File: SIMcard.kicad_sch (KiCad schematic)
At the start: 9 parts, among them J8 1042240820

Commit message: Dual SIM version
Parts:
- renumbered R27 to R23, R28 to R24, R29 to R25
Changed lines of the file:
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@@
 		(in_pos_files yes)
 		(dnp no)
-		(property "Reference" "R27"
+		(property "Reference" "R23"
 			(at 134.112 71.12 90)
 			(show_name no)
@@
 			(project "GSMreceiver"
 				(path "/bbc92722-7b85-49e8-a662-589426df605a/0766f5ef-5d4e-4bb3-b73a-d8d6c795d8e3"
-					(reference "R30")
+					(reference "R26")
 					(unit 1)
 				)
 				(path "/bbc92722-7b85-49e8-a662-589426df605a/89f536d0-e840-48e9-a183-c973796594df"
-					(reference "R27")
+					(reference "R23")
 					(unit 1)
 				)
@@
 		(in_pos_files yes)
 		(dnp no)
-		(property "Reference" "R28"
+		(property "Reference" "R24"
 			(at 134.62 76.2 90)
 			(show_name no)
@@
 			(project "GSMreceiver"
 				(path "/bbc92722-7b85-49e8-a662-589426df605a/0766f5ef-5d4e-4bb3-b73a-d8d6c795d8e3"
-					(reference "R31")
+					(reference "R27")
 					(unit 1)
 				)
 				(path "/bbc92722-7b85-49e8-a662-589426df605a/89f536d0-e840-48e9-a183-c973796594df"
-					(reference "R28")
+					(reference "R24")
 					(unit 1)
 				)
@@
 		(in_pos_files yes)
 		(dnp no)
-		(property "Reference" "R29"
+		(property "Reference" "R25"
 			(at 134.62 81.28 90)
 			(show_name no)
@@
 			(project "GSMreceiver"
 				(path "/bbc92722-7b85-49e8-a662-589426df605a/0766f5ef-5d4e-4bb3-b73a-d8d6c795d8e3"
-					(reference "R32")
+					(reference "R28")
 					(unit 1)
 				)
 				(path "/bbc92722-7b85-49e8-a662-589426df605a/89f536d0-e840-48e9-a183-c973796594df"
-					(reference "R29")
-					(unit 1)
-				)
+					(reference "R25")
+					(unit 1)
+				)

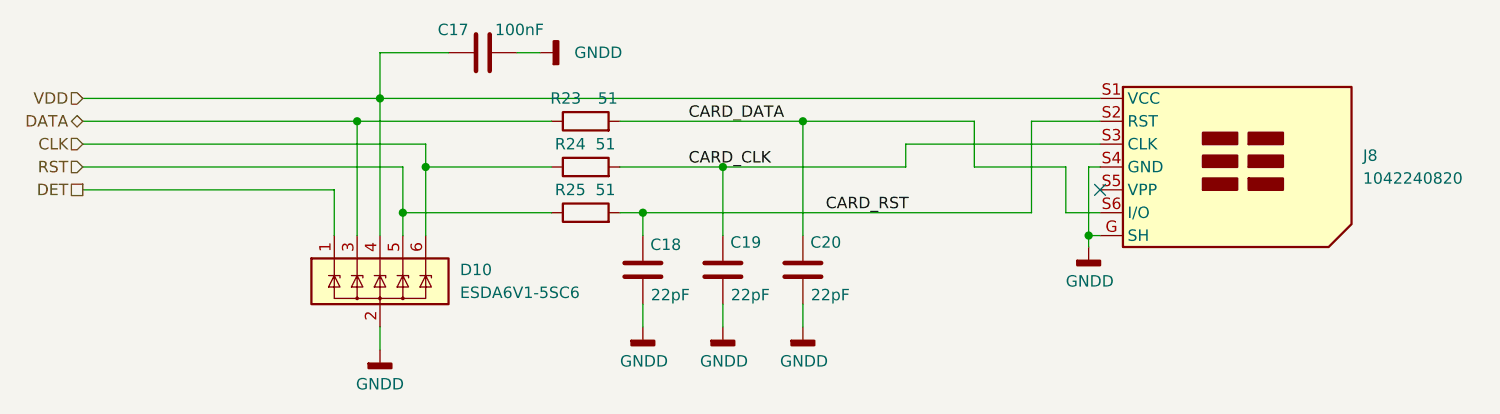
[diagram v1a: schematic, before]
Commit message: Replace SIM800C-DS with A7682E
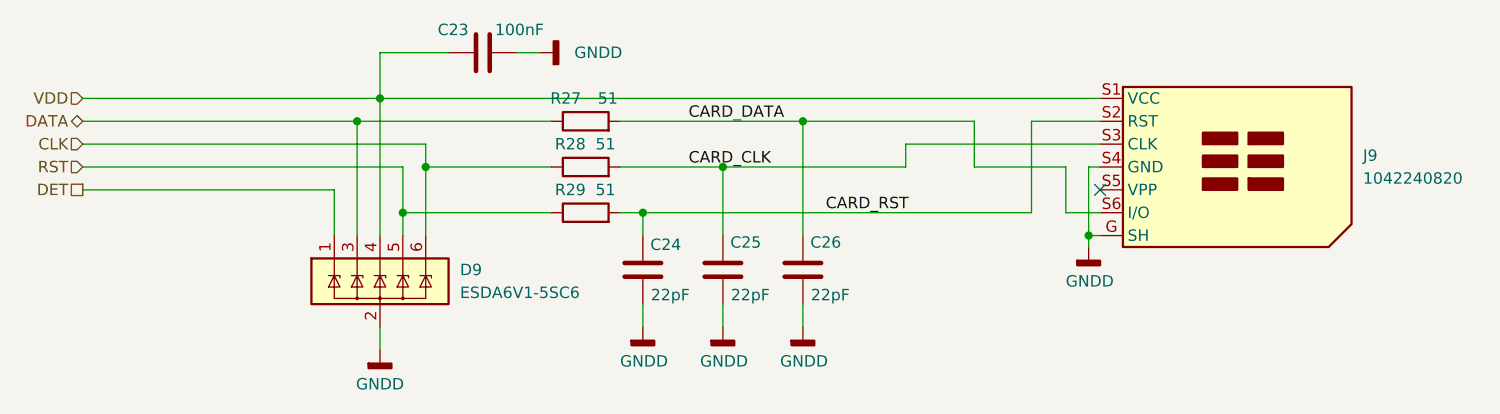
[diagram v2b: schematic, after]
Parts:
- renumbered C17 to C23, C18 to C24, C19 to C25, C20 to C26, D10 to D9, J8 to J9, R23 to R27, R24 to R28, R25 to R29
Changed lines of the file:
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@@
 		(in_pos_files yes)
 		(dnp no)
-		(property "Reference" "R23"
+		(property "Reference" "R27"
 			(at 134.112 71.12 90)
 			(show_name no)
@@
 			(project "GSMreceiver"
 				(path "/bbc92722-7b85-49e8-a662-589426df605a/0766f5ef-5d4e-4bb3-b73a-d8d6c795d8e3"
-					(reference "R26")
+					(reference "R30")
 					(unit 1)
 				)
 				(path "/bbc92722-7b85-49e8-a662-589426df605a/89f536d0-e840-48e9-a183-c973796594df"
-					(reference "R23")
+					(reference "R27")
 					(unit 1)
 				)
@@
 		(dnp no)
 		(fields_autoplaced yes)
-		(property "Reference" "#PWR038"
+		(property "Reference" "#PWR042"
 			(at 111.76 105.41 0)
 			(hide yes)
@@
 			(project "GSMreceiver"
 				(path "/bbc92722-7b85-49e8-a662-589426df605a/0766f5ef-5d4e-4bb3-b73a-d8d6c795d8e3"
-					(reference "#PWR044")
+					(reference "#PWR048")
 					(unit 1)
 				)
 				(path "/bbc92722-7b85-49e8-a662-589426df605a/89f536d0-e840-48e9-a183-c973796594df"
-					(reference "#PWR038")
+					(reference "#PWR042")
 					(unit 1)
 				)
@@
 		(in_pos_files yes)
 		(dnp no)
-		(property "Reference" "R24"
+		(property "Reference" "R28"
 			(at 134.62 76.2 90)
 			(show_name no)
@@
 			(project "GSMreceiver"
 				(path "/bbc92722-7b85-49e8-a662-589426df605a/0766f5ef-5d4e-4bb3-b73a-d8d6c795d8e3"
-					(reference "R27")
+					(reference "R31")
 					(unit 1)
 				)
 				(path "/bbc92722-7b85-49e8-a662-589426df605a/89f536d0-e840-48e9-a183-c973796594df"
-					(reference "R24")
+					(reference "R28")
 					(unit 1)
 				)
@@
 		(in_pos_files yes)
 		(dnp no)
-		(property "Reference" "#PWR043"
+		(property "Reference" "#PWR047"
 			(at 190.5 93.98 0)
 			(hide yes)
@@
 			(project "GSMreceiver"
 				(path "/bbc92722-7b85-49e8-a662-589426df605a/0766f5ef-5d4e-4bb3-b73a-d8d6c795d8e3"
-					(reference "#PWR049")
+					(reference "#PWR053")
 					(unit 1)
 				)
 				(path "/bbc92722-7b85-49e8-a662-589426df605a/89f536d0-e840-48e9-a183-c973796594df"
-					(reference "#PWR043")
+					(reference "#PWR047")
 					(unit 1)
 				)
@@
 		(dnp no)
 		(fields_autoplaced yes)
-		(property "Reference" "J8"
+		(property "Reference" "J9"
 			(at 220.98 77.4699 0)
 			(show_name no)
@@
 			(project "GSMreceiver"
 				(path "/bbc92722-7b85-49e8-a662-589426df605a/0766f5ef-5d4e-4bb3-b73a-d8d6c795d8e3"
+					(reference "J10")
+					(unit 1)
+				)
+				(path "/bbc92722-7b85-49e8-a662-589426df605a/89f536d0-e840-48e9-a183-c973796594df"
 					(reference "J9")
-					(unit 1)
-				)
-				(path "/bbc92722-7b85-49e8-a662-589426df605a/89f536d0-e840-48e9-a183-c973796594df"
-					(reference "J8")
 					(unit 1)
 				)
@@
 		(in_pos_files yes)
 		(dnp no)
-		(property "Reference" "#PWR042"
+		(property "Reference" "#PWR046"
 			(at 158.75 102.87 0)
 			(hide yes)
@@
 			(project "GSMreceiver"
 				(path "/bbc92722-7b85-49e8-a662-589426df605a/0766f5ef-5d4e-4bb3-b73a-d8d6c795d8e3"
-					(reference "#PWR048")
+					(reference "#PWR052")
 					(unit 1)
 				)
 				(path "/bbc92722-7b85-49e8-a662-589426df605a/89f536d0-e840-48e9-a183-c973796594df"
-					(reference "#PWR042")
+					(reference "#PWR046")
 					(unit 1)
 				)
@@
 		(in_pos_files yes)
 		(dnp no)
-		(property "Reference" "C19"
+		(property "Reference" "C25"
 			(at 152.4 87.122 0)
 			(show_name no)
@@
 			(project "GSMreceiver"
 				(path "/bbc92722-7b85-49e8-a662-589426df605a/0766f5ef-5d4e-4bb3-b73a-d8d6c795d8e3"
-					(reference "C23")
+					(reference "C29")
 					(unit 1)
 				)
 				(path "/bbc92722-7b85-49e8-a662-589426df605a/89f536d0-e840-48e9-a183-c973796594df"
-					(reference "C19")
+					(reference "C25")
 					(unit 1)
 				)
@@
 		(dnp no)
 		(fields_autoplaced yes)
-		(property "Reference" "#PWR039"
+		(property "Reference" "#PWR043"
 			(at 135.89 66.04 0)
 			(hide yes)
@@
 			(project "GSMreceiver"
 				(path "/bbc92722-7b85-49e8-a662-589426df605a/0766f5ef-5d4e-4bb3-b73a-d8d6c795d8e3"
-					(reference "#PWR045")
+					(reference "#PWR049")
 					(unit 1)
 				)
 				(path "/bbc92722-7b85-49e8-a662-589426df605a/89f536d0-e840-48e9-a183-c973796594df"
-					(reference "#PWR039")
+					(reference "#PWR043")
 					(unit 1)
 				)
@@
 		(in_pos_files yes)
 		(dnp no)
-		(property "Reference" "C17"
+		(property "Reference" "C23"
 			(at 119.888 63.5 90)
 			(show_name no)
@@
 			(project "GSMreceiver"
 				(path "/bbc92722-7b85-49e8-a662-589426df605a/0766f5ef-5d4e-4bb3-b73a-d8d6c795d8e3"
-					(reference "C21")
+					(reference "C27")
 					(unit 1)
 				)
 				(path "/bbc92722-7b85-49e8-a662-589426df605a/89f536d0-e840-48e9-a183-c973796594df"
-					(reference "C17")
+					(reference "C23")
 					(unit 1)
 				)
@@
 		(in_pos_files yes)
 		(dnp no)
-		(property "Reference" "C18"
+		(property "Reference" "C24"
 			(at 143.51 87.376 0)
 			(show_name no)
@@
 			(project "GSMreceiver"
 				(path "/bbc92722-7b85-49e8-a662-589426df605a/0766f5ef-5d4e-4bb3-b73a-d8d6c795d8e3"
-					(reference "C22")
+					(reference "C28")
 					(unit 1)
 				)
 				(path "/bbc92722-7b85-49e8-a662-589426df605a/89f536d0-e840-48e9-a183-c973796594df"
-					(reference "C18")
+					(reference "C24")
 					(unit 1)
 				)
@@
 		(dnp no)
 		(fields_autoplaced yes)
-		(property "Reference" "D10"
+		(property "Reference" "D9"
 			(at 120.65 90.1699 0)
 			(show_name no)
@@
 			(project "GSMreceiver"
 				(path "/bbc92722-7b85-49e8-a662-589426df605a/0766f5ef-5d4e-4bb3-b73a-d8d6c795d8e3"
-					(reference "D11")
+					(reference "D10")
 					(unit 1)
 				)
 				(path "/bbc92722-7b85-49e8-a662-589426df605a/89f536d0-e840-48e9-a183-c973796594df"
-					(reference "D10")
+					(reference "D9")
 					(unit 1)
 				)
@@
 		(in_pos_files yes)
 		(dnp no)
-		(property "Reference" "#PWR041"
+		(property "Reference" "#PWR045"
 			(at 149.86 102.87 0)
 			(hide yes)
@@
 			(project "GSMreceiver"
 				(path "/bbc92722-7b85-49e8-a662-589426df605a/0766f5ef-5d4e-4bb3-b73a-d8d6c795d8e3"
-					(reference "#PWR047")
+					(reference "#PWR051")
 					(unit 1)
 				)
 				(path "/bbc92722-7b85-49e8-a662-589426df605a/89f536d0-e840-48e9-a183-c973796594df"
-					(reference "#PWR041")
+					(reference "#PWR045")
 					(unit 1)
 				)
@@
 		(in_pos_files yes)
 		(dnp no)
-		(property "Reference" "C20"
+		(property "Reference" "C26"
 			(at 161.29 87.122 0)
 			(show_name no)
@@
 			(project "GSMreceiver"
 				(path "/bbc92722-7b85-49e8-a662-589426df605a/0766f5ef-5d4e-4bb3-b73a-d8d6c795d8e3"
-					(reference "C24")
+					(reference "C30")
 					(unit 1)
 				)
 				(path "/bbc92722-7b85-49e8-a662-589426df605a/89f536d0-e840-48e9-a183-c973796594df"
-					(reference "C20")
+					(reference "C26")
 					(unit 1)
 				)
@@
 		(in_pos_files yes)
 		(dnp no)
-		(property "Reference" "#PWR040"
+		(property "Reference" "#PWR044"
 			(at 140.97 102.87 0)
 			(hide yes)
@@
 			(project "GSMreceiver"
 				(path "/bbc92722-7b85-49e8-a662-589426df605a/0766f5ef-5d4e-4bb3-b73a-d8d6c795d8e3"
-					(reference "#PWR046")
+					(reference "#PWR050")
 					(unit 1)
 				)
 				(path "/bbc92722-7b85-49e8-a662-589426df605a/89f536d0-e840-48e9-a183-c973796594df"
-					(reference "#PWR040")
+					(reference "#PWR044")
 					(unit 1)
 				)
@@
 		(in_pos_files yes)
 		(dnp no)
-		(property "Reference" "R25"
+		(property "Reference" "R29"
 			(at 134.62 81.28 90)
 			(show_name no)
@@
 			(project "GSMreceiver"
 				(path "/bbc92722-7b85-49e8-a662-589426df605a/0766f5ef-5d4e-4bb3-b73a-d8d6c795d8e3"
-					(reference "R28")
+					(reference "R32")
 					(unit 1)
 				)
 				(path "/bbc92722-7b85-49e8-a662-589426df605a/89f536d0-e840-48e9-a183-c973796594df"
-					(reference "R25")
-					(unit 1)
-				)
+					(reference "R29")
+					(unit 1)
+				)

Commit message: USB connector inversion fix
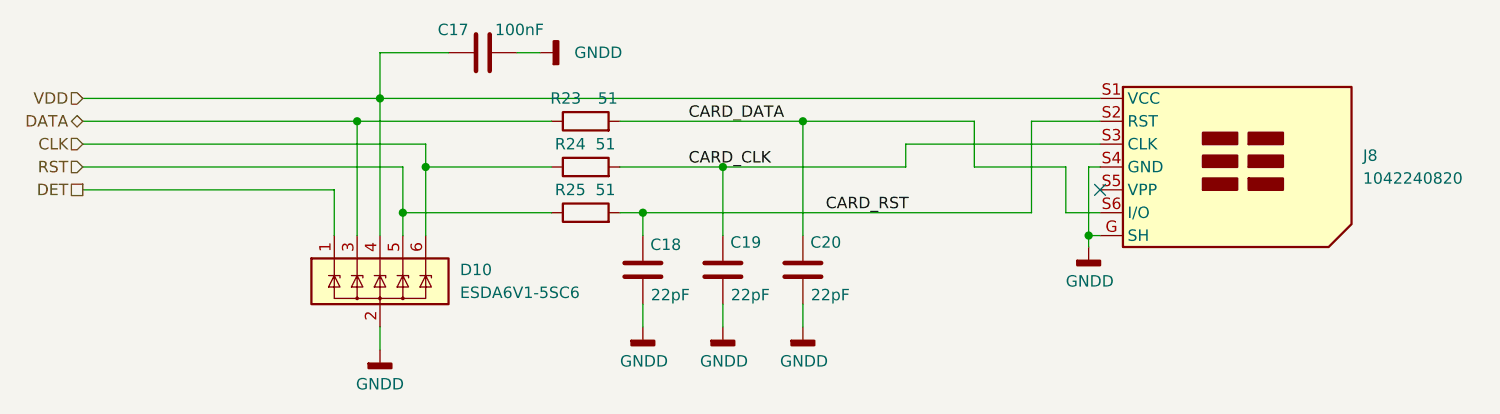
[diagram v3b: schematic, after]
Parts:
- renumbered C23 to C17, C24 to C18, C25 to C19, C26 to C20, D9 to D10, J9 to J8, R27 to R23, R28 to R24, R29 to R25
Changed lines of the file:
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@@
 		(in_pos_files yes)
 		(dnp no)
-		(property "Reference" "R27"
+		(property "Reference" "R23"
 			(at 134.112 71.12 90)
 			(show_name no)
@@
 			(project "GSMreceiver"
 				(path "/bbc92722-7b85-49e8-a662-589426df605a/0766f5ef-5d4e-4bb3-b73a-d8d6c795d8e3"
-					(reference "R30")
+					(reference "R26")
 					(unit 1)
 				)
 				(path "/bbc92722-7b85-49e8-a662-589426df605a/89f536d0-e840-48e9-a183-c973796594df"
-					(reference "R27")
+					(reference "R23")
 					(unit 1)
 				)
@@
 		(dnp no)
 		(fields_autoplaced yes)
-		(property "Reference" "#PWR042"
+		(property "Reference" "#PWR038"
 			(at 111.76 105.41 0)
 			(hide yes)
@@
 			(project "GSMreceiver"
 				(path "/bbc92722-7b85-49e8-a662-589426df605a/0766f5ef-5d4e-4bb3-b73a-d8d6c795d8e3"
-					(reference "#PWR048")
+					(reference "#PWR044")
 					(unit 1)
 				)
 				(path "/bbc92722-7b85-49e8-a662-589426df605a/89f536d0-e840-48e9-a183-c973796594df"
-					(reference "#PWR042")
+					(reference "#PWR038")
 					(unit 1)
 				)
@@
 		(in_pos_files yes)
 		(dnp no)
-		(property "Reference" "R28"
+		(property "Reference" "R24"
 			(at 134.62 76.2 90)
 			(show_name no)
@@
 			(project "GSMreceiver"
 				(path "/bbc92722-7b85-49e8-a662-589426df605a/0766f5ef-5d4e-4bb3-b73a-d8d6c795d8e3"
-					(reference "R31")
+					(reference "R27")
 					(unit 1)
 				)
 				(path "/bbc92722-7b85-49e8-a662-589426df605a/89f536d0-e840-48e9-a183-c973796594df"
-					(reference "R28")
+					(reference "R24")
 					(unit 1)
 				)
@@
 		(in_pos_files yes)
 		(dnp no)
-		(property "Reference" "#PWR047"
+		(property "Reference" "#PWR043"
 			(at 190.5 93.98 0)
 			(hide yes)
@@
 			(project "GSMreceiver"
 				(path "/bbc92722-7b85-49e8-a662-589426df605a/0766f5ef-5d4e-4bb3-b73a-d8d6c795d8e3"
-					(reference "#PWR053")
+					(reference "#PWR049")
 					(unit 1)
 				)
 				(path "/bbc92722-7b85-49e8-a662-589426df605a/89f536d0-e840-48e9-a183-c973796594df"
-					(reference "#PWR047")
+					(reference "#PWR043")
 					(unit 1)
 				)
@@
 		(dnp no)
 		(fields_autoplaced yes)
-		(property "Reference" "J9"
+		(property "Reference" "J8"
 			(at 220.98 77.4699 0)
 			(show_name no)
@@
 			(project "GSMreceiver"
 				(path "/bbc92722-7b85-49e8-a662-589426df605a/0766f5ef-5d4e-4bb3-b73a-d8d6c795d8e3"
-					(reference "J10")
+					(reference "J9")
 					(unit 1)
 				)
 				(path "/bbc92722-7b85-49e8-a662-589426df605a/89f536d0-e840-48e9-a183-c973796594df"
-					(reference "J9")
+					(reference "J8")
 					(unit 1)
 				)
@@
 		(in_pos_files yes)
 		(dnp no)
-		(property "Reference" "#PWR046"
+		(property "Reference" "#PWR042"
 			(at 158.75 102.87 0)
 			(hide yes)
@@
 			(project "GSMreceiver"
 				(path "/bbc92722-7b85-49e8-a662-589426df605a/0766f5ef-5d4e-4bb3-b73a-d8d6c795d8e3"
-					(reference "#PWR052")
+					(reference "#PWR048")
 					(unit 1)
 				)
 				(path "/bbc92722-7b85-49e8-a662-589426df605a/89f536d0-e840-48e9-a183-c973796594df"
-					(reference "#PWR046")
+					(reference "#PWR042")
 					(unit 1)
 				)
@@
 		(in_pos_files yes)
 		(dnp no)
-		(property "Reference" "C25"
+		(property "Reference" "C19"
 			(at 152.4 87.122 0)
 			(show_name no)
@@
 			(project "GSMreceiver"
 				(path "/bbc92722-7b85-49e8-a662-589426df605a/0766f5ef-5d4e-4bb3-b73a-d8d6c795d8e3"
-					(reference "C29")
+					(reference "C23")
 					(unit 1)
 				)
 				(path "/bbc92722-7b85-49e8-a662-589426df605a/89f536d0-e840-48e9-a183-c973796594df"
-					(reference "C25")
+					(reference "C19")
 					(unit 1)
 				)
@@
 		(dnp no)
 		(fields_autoplaced yes)
-		(property "Reference" "#PWR043"
+		(property "Reference" "#PWR039"
 			(at 135.89 66.04 0)
 			(hide yes)
@@
 			(project "GSMreceiver"
 				(path "/bbc92722-7b85-49e8-a662-589426df605a/0766f5ef-5d4e-4bb3-b73a-d8d6c795d8e3"
-					(reference "#PWR049")
+					(reference "#PWR045")
 					(unit 1)
 				)
 				(path "/bbc92722-7b85-49e8-a662-589426df605a/89f536d0-e840-48e9-a183-c973796594df"
-					(reference "#PWR043")
+					(reference "#PWR039")
 					(unit 1)
 				)
@@
 		(in_pos_files yes)
 		(dnp no)
-		(property "Reference" "C23"
+		(property "Reference" "C17"
 			(at 119.888 63.5 90)
 			(show_name no)
@@
 			(project "GSMreceiver"
 				(path "/bbc92722-7b85-49e8-a662-589426df605a/0766f5ef-5d4e-4bb3-b73a-d8d6c795d8e3"
-					(reference "C27")
+					(reference "C21")
 					(unit 1)
 				)
 				(path "/bbc92722-7b85-49e8-a662-589426df605a/89f536d0-e840-48e9-a183-c973796594df"
-					(reference "C23")
+					(reference "C17")
 					(unit 1)
 				)
@@
 		(in_pos_files yes)
 		(dnp no)
-		(property "Reference" "C24"
+		(property "Reference" "C18"
 			(at 143.51 87.376 0)
 			(show_name no)
@@
 			(project "GSMreceiver"
 				(path "/bbc92722-7b85-49e8-a662-589426df605a/0766f5ef-5d4e-4bb3-b73a-d8d6c795d8e3"
-					(reference "C28")
+					(reference "C22")
 					(unit 1)
 				)
 				(path "/bbc92722-7b85-49e8-a662-589426df605a/89f536d0-e840-48e9-a183-c973796594df"
-					(reference "C24")
+					(reference "C18")
 					(unit 1)
 				)
@@
 		(dnp no)
 		(fields_autoplaced yes)
-		(property "Reference" "D9"
+		(property "Reference" "D10"
 			(at 120.65 90.1699 0)
 			(show_name no)
@@
 			(project "GSMreceiver"
 				(path "/bbc92722-7b85-49e8-a662-589426df605a/0766f5ef-5d4e-4bb3-b73a-d8d6c795d8e3"
+					(reference "D11")
+					(unit 1)
+				)
+				(path "/bbc92722-7b85-49e8-a662-589426df605a/89f536d0-e840-48e9-a183-c973796594df"
 					(reference "D10")
-					(unit 1)
-				)
-				(path "/bbc92722-7b85-49e8-a662-589426df605a/89f536d0-e840-48e9-a183-c973796594df"
-					(reference "D9")
 					(unit 1)
 				)
@@
 		(in_pos_files yes)
 		(dnp no)
-		(property "Reference" "#PWR045"
+		(property "Reference" "#PWR041"
 			(at 149.86 102.87 0)
 			(hide yes)
@@
 			(project "GSMreceiver"
 				(path "/bbc92722-7b85-49e8-a662-589426df605a/0766f5ef-5d4e-4bb3-b73a-d8d6c795d8e3"
-					(reference "#PWR051")
+					(reference "#PWR047")
 					(unit 1)
 				)
 				(path "/bbc92722-7b85-49e8-a662-589426df605a/89f536d0-e840-48e9-a183-c973796594df"
-					(reference "#PWR045")
+					(reference "#PWR041")
 					(unit 1)
 				)
@@
 		(in_pos_files yes)
 		(dnp no)
-		(property "Reference" "C26"
+		(property "Reference" "C20"
 			(at 161.29 87.122 0)
 			(show_name no)
@@
 			(project "GSMreceiver"
 				(path "/bbc92722-7b85-49e8-a662-589426df605a/0766f5ef-5d4e-4bb3-b73a-d8d6c795d8e3"
-					(reference "C30")
+					(reference "C24")
 					(unit 1)
 				)
 				(path "/bbc92722-7b85-49e8-a662-589426df605a/89f536d0-e840-48e9-a183-c973796594df"
-					(reference "C26")
+					(reference "C20")
 					(unit 1)
 				)
@@
 		(in_pos_files yes)
 		(dnp no)
-		(property "Reference" "#PWR044"
+		(property "Reference" "#PWR040"
 			(at 140.97 102.87 0)
 			(hide yes)
@@
 			(project "GSMreceiver"
 				(path "/bbc92722-7b85-49e8-a662-589426df605a/0766f5ef-5d4e-4bb3-b73a-d8d6c795d8e3"
-					(reference "#PWR050")
+					(reference "#PWR046")
 					(unit 1)
 				)
 				(path "/bbc92722-7b85-49e8-a662-589426df605a/89f536d0-e840-48e9-a183-c973796594df"
-					(reference "#PWR044")
+					(reference "#PWR040")
 					(unit 1)
 				)
@@
 		(in_pos_files yes)
 		(dnp no)
-		(property "Reference" "R29"
+		(property "Reference" "R25"
 			(at 134.62 81.28 90)
 			(show_name no)
@@
 			(project "GSMreceiver"
 				(path "/bbc92722-7b85-49e8-a662-589426df605a/0766f5ef-5d4e-4bb3-b73a-d8d6c795d8e3"
-					(reference "R32")
+					(reference "R28")
 					(unit 1)
 				)
 				(path "/bbc92722-7b85-49e8-a662-589426df605a/89f536d0-e840-48e9-a183-c973796594df"
-					(reference "R29")
-					(unit 1)
-				)
+					(reference "R25")
+					(unit 1)
+				)
